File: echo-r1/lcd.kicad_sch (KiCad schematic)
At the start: 8 parts, among them J6 AFD01-S35FCC-00, U10 SY7200A

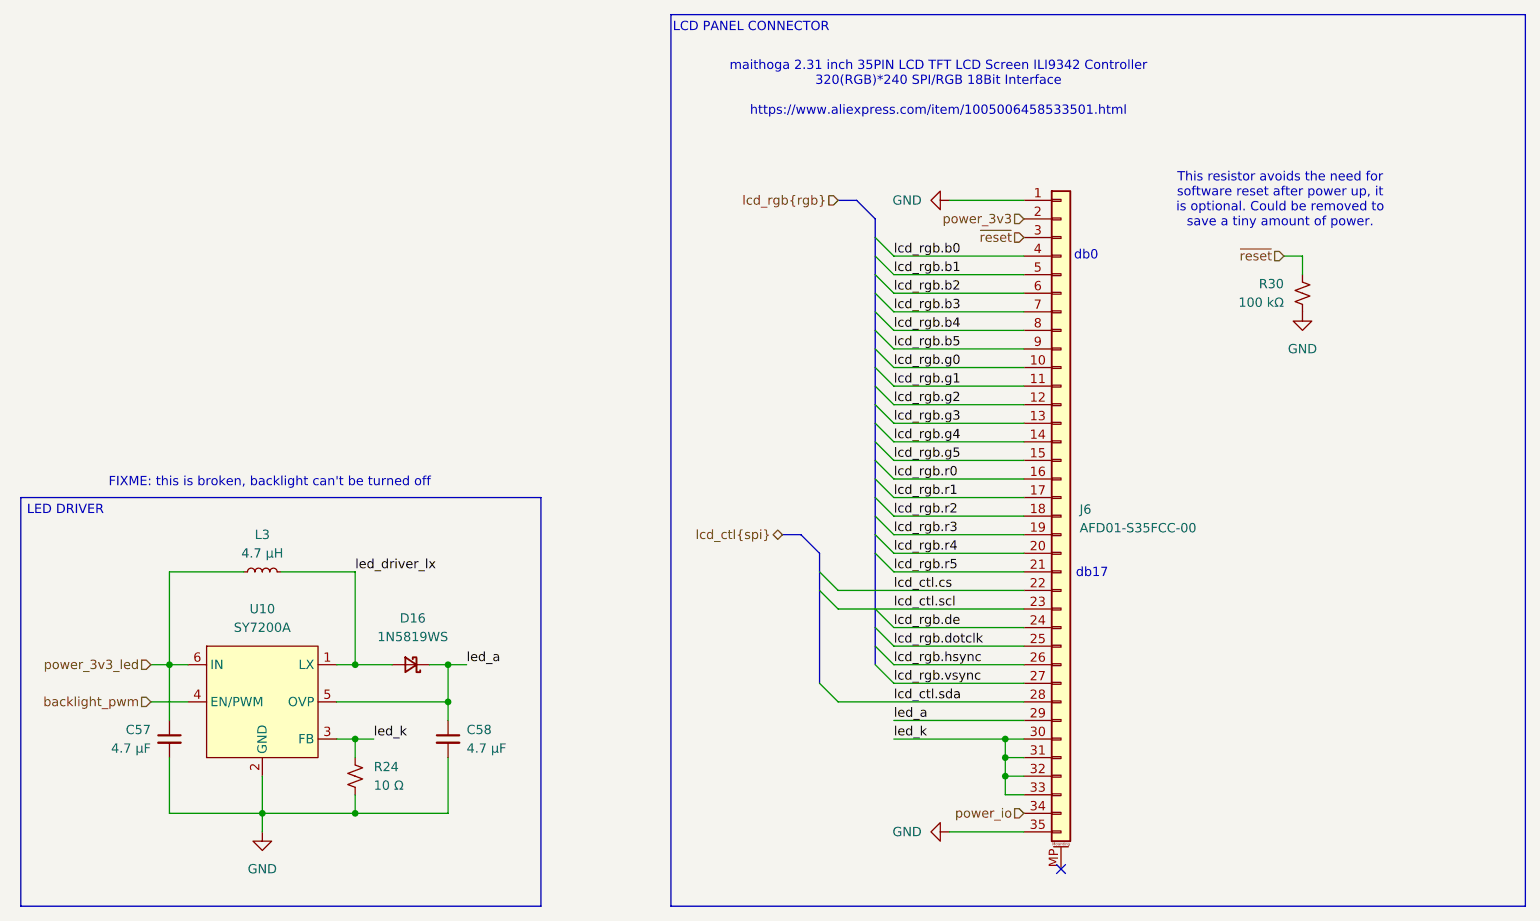
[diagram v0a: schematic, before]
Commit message: R1-Rev1: replace SY7200A LED driver with AP2502 current limiter
The SY7200A is a boost converter designed for series LED
strings, which require a high drive voltage. The external
circuitry allows some input power to pass through to the
output -- which is normally not a problem for LED strings
because this low voltage is not enough to overcome their
combined voltage drop.

However, the LCD uses 4 LEDs in parallel, and this low
voltage is enough to light the LEDs while the converter
is disabled, so the backlight can't be turned off.

Fix this by using the AP2502 4-channel current limiter
instead, which is basically a low side switch. LEDs are
powered directly from 3.3V, and each is independently
switched through the AP2502.
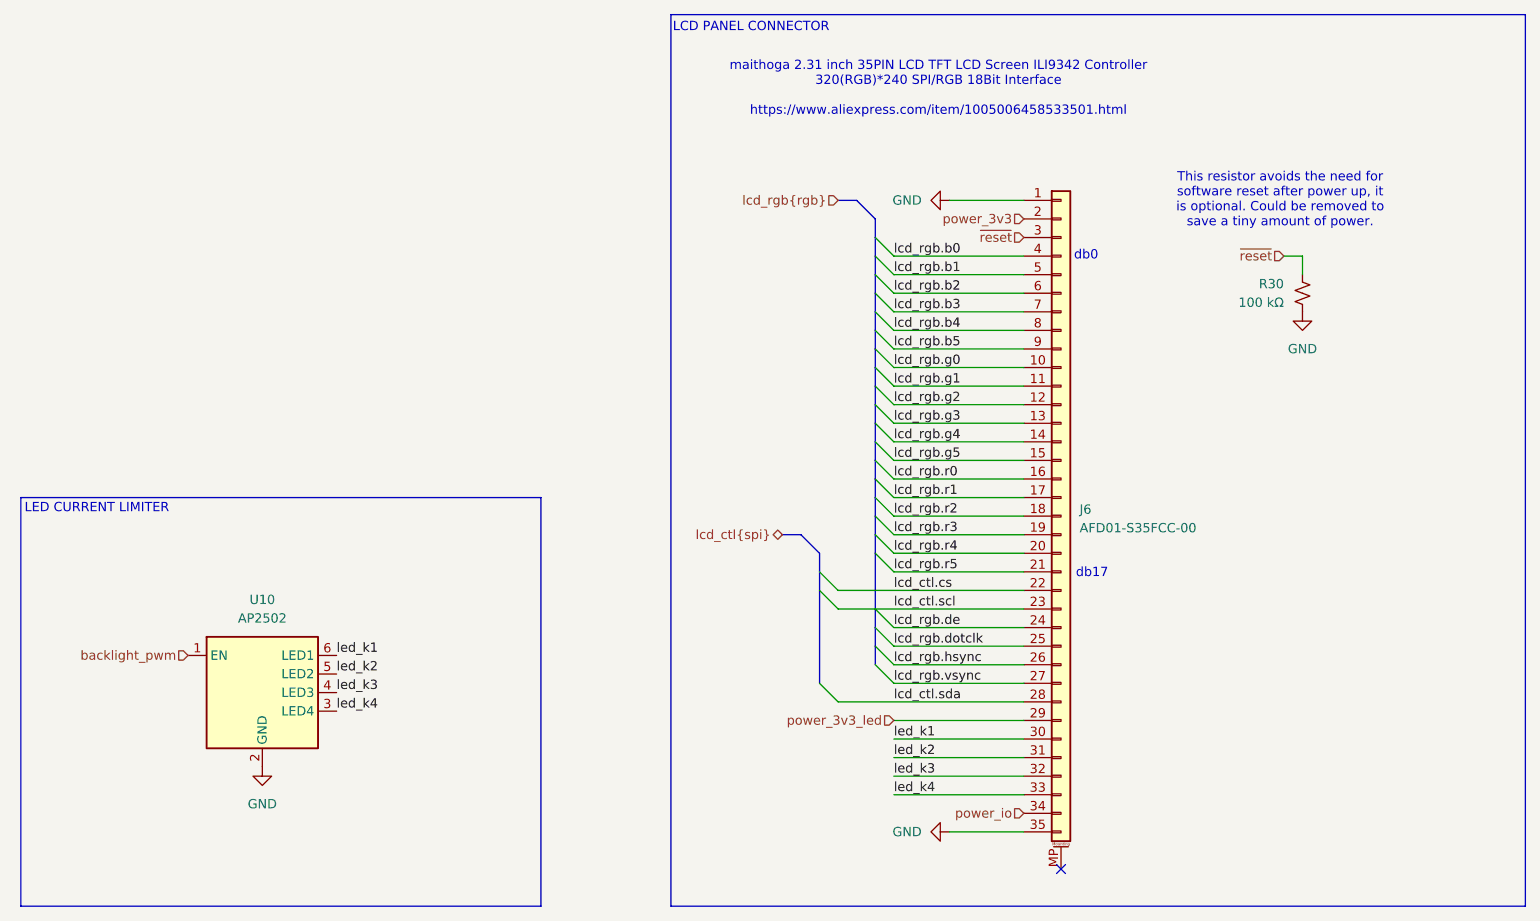
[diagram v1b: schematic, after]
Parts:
- removed C57, C58: 4.7 µF, Capacitor_SMD:C_0603_1608Metric, symbol Device:C_Small
- removed D16: 1N5819WS, Diode_SMD:D_SOD-323, symbol Device:D_Schottky_Small
- removed L3: 4.7 µH, echoplayer:L_0806_2016Metric, symbol Device:L_Small
- removed R24: 10 Ω, Resistor_SMD:R_0402_1005Metric, symbol Device:R_Small_US
- removed U10: SY7200A, Package_TO_SOT_SMD:SOT-23-6, symbol echoplayer:SY7200A
- added U10: AP2502, Package_TO_SOT_SMD:SOT-23-6, symbol echoplayer:AP2502
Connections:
- net led_a is gone; now on net power_3v3_led: J6.29 (Pin_29)
- net GND: now also U10.2 (GND)
- net backlight_pwm: now also U10.1 (EN)
- removed net led_k: J6.30 (Pin_30), J6.31 (Pin_31), J6.32 (Pin_32), J6.33 (Pin_33)
- new net led_k1: J6.30 (Pin_30), U10.6 (LED1)
- new net led_k2: J6.31 (Pin_31), U10.5 (LED2)
- new net led_k3: J6.32 (Pin_32), U10.4 (LED3)
- new net led_k4: J6.33 (Pin_33), U10.3 (LED4)
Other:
- note added: "LED CURRENT LIMITER"
- note removed: "FIXME: this is broken, backlight can't be turned off"
- note removed: "LED DRIVER"

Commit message: WIP redesign with STM32H7R3Z8J6
The H7R3 has a bunch of features that greatly simplify the design:
support for HyperRAM, which requires far fewer pins than SDRAM and
is more power efficient; this frees up the FMC to interface with the
display in 8-bit 8080 MCU mode; and there is a built-in USB HS PHY,
removing the need for an external PHY.

The huge reduction in signal count allows for a smaller pin count
package -- only 144 pins. HyperRAM only comes in BGA packages so it
makes sense to also use the UFBGA-144 package for the CPU, which
takes up less than 1/4 of the board area of an LQFP-176 package.
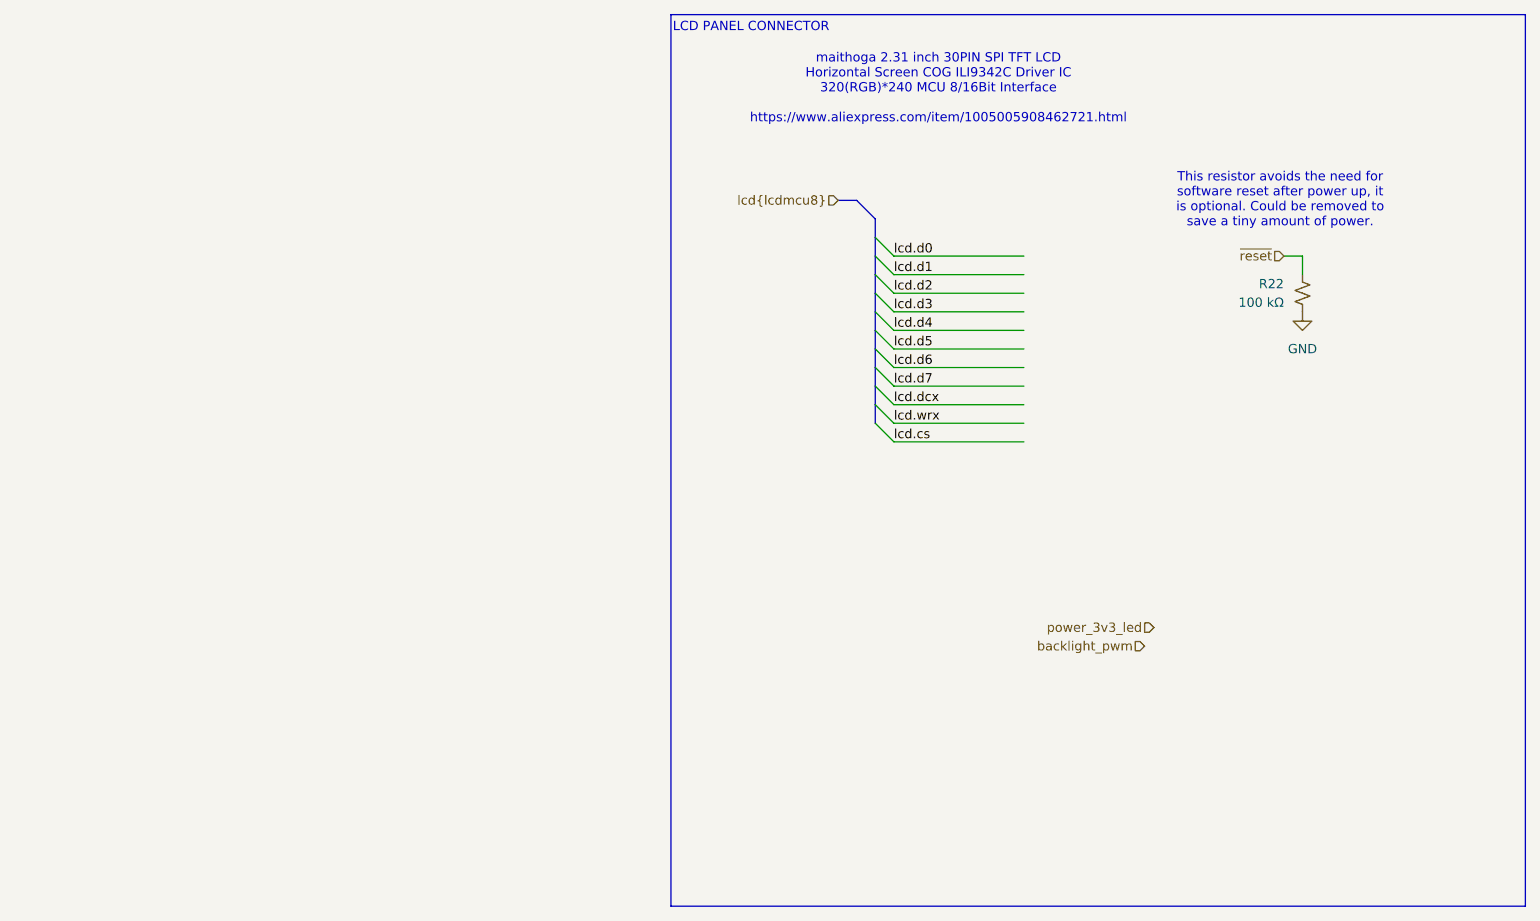
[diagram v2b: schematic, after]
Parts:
- removed J6: AFD01-S35FCC-00, echoplayer:Conn_Jushuo_AFD01-S35FCC-00_RTL, symbol Connector_Generic_MountingPin:Conn_01x35_MountingPin
- removed U10: AP2502, Package_TO_SOT_SMD:SOT-23-6, symbol echoplayer:AP2502
- renumbered R30 to R22
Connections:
- no-connect marks 1 -> 0
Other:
- note added: "maithoga 2.31 inch 30PIN SPI TFT LCD Horizontal Screen COG ILI9342C Driver IC 320(RGB)*240 MCU 8/16Bit Interface https://www.aliexpress.com/item/1005005908462721.html"
- note removed: "LED CURRENT LIMITER"
- note removed: "db0"
- note removed: "db17"
- note removed: "maithoga 2.31 inch 35PIN LCD TFT LCD Screen ILI9342 Controller 320(RGB)*240 SPI/RGB 18Bit Interface https://www.aliexpress.com/item/1005006458533501.html"
